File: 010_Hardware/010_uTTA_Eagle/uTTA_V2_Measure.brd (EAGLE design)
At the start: 100.4 x 79 mm, 304 parts, among them IC101.1 LT1167, IC101.2 LT1167, IC101.3 LT1167, IC101.4 LT1167, IC151.1 MCP602SN, IC151.3 MCP602SN, IC301 AD5664, IC302 LT1004CLP-2.5, IC303 TL074D, IC351.1 OPA2156ID, IC351.2 OPA2156ID, IC351.3 OPA2156ID, IC351.4 OPA2156ID, IC601.1 MAX6675ISA, IC601.2 MAX6675ISA, IC601.3 MAX6675ISA, IC601.4 MAX6675ISA, T151 BSS138PS, U11 NUCLEO_F103_BOT, U121.1 W25Q128JV, U121.2 W25Q128JV, X101.1 BU-SMA-GSPECIAL, X101.2 BU-SMA-GSPECIAL, X101.3 BU-SMA-GSPECIAL, X101.4 BU-SMA-GSPECIAL

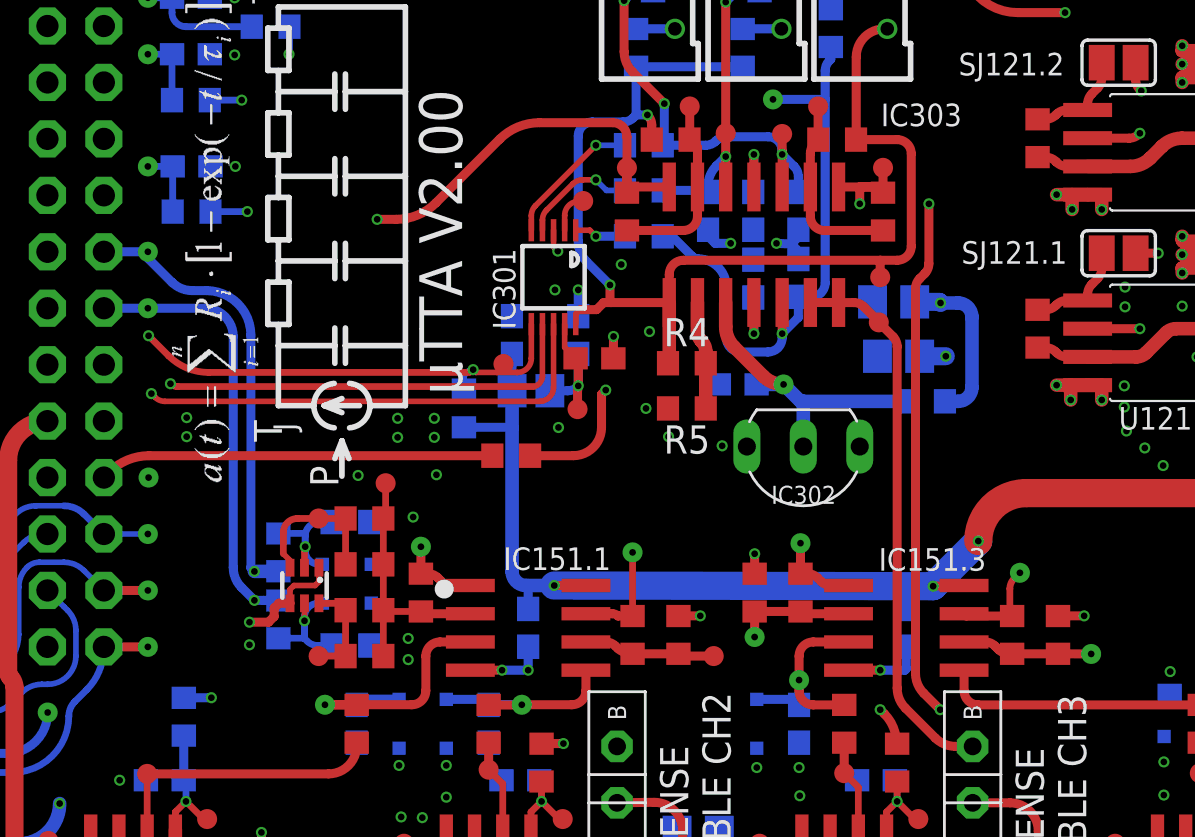
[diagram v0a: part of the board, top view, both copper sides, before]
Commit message: Optimization of Testpoints for Calibration
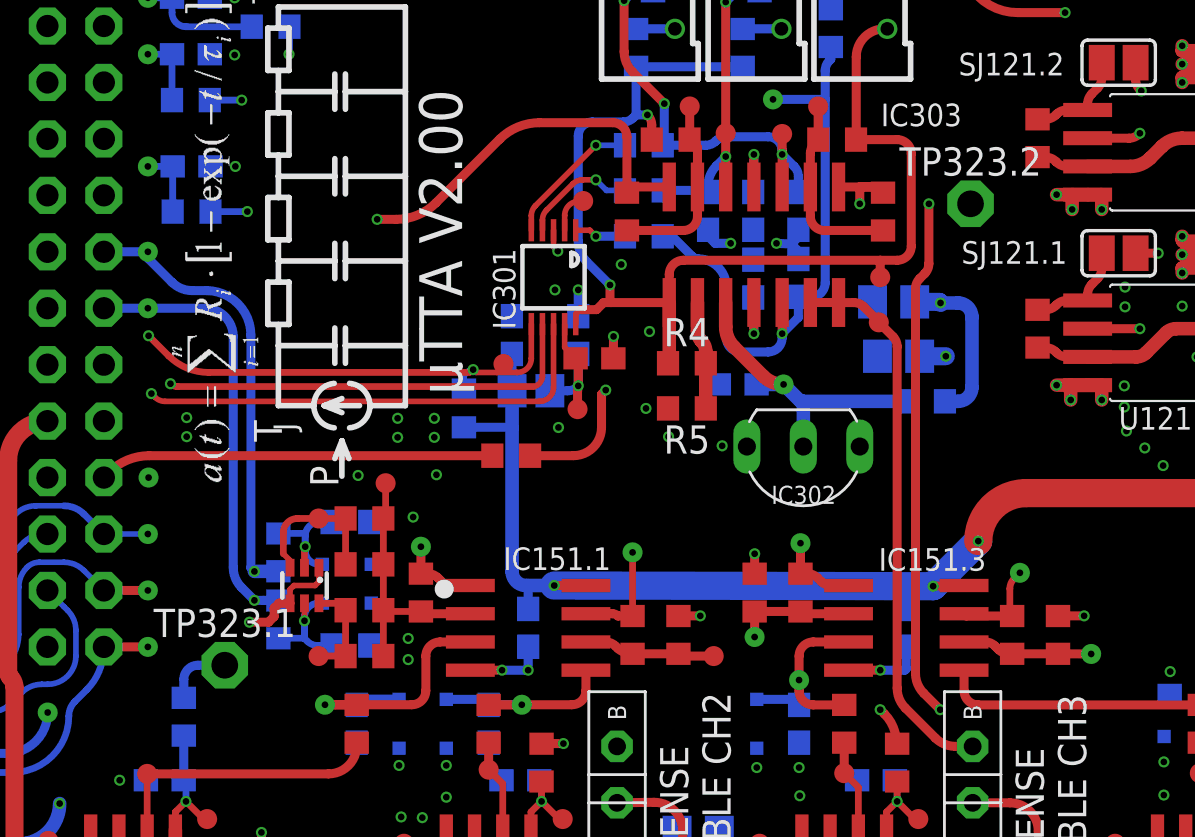
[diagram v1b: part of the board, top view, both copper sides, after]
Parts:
- IC351.1, IC351.2, IC351.3, IC351.4: value OPA2156ID -> AD8672ARZ
- R326.1, R326.2: value 2k -> 4k99
- TP1, TP101.1, TP101.2, TP101.3, TP101.4, TP102.1, TP102.2, TP102.3, TP102.4, TP103.1, TP103.2, TP103.3, TP103.4, TP104.1, TP104.2, TP104.3, TP104.4, TP105.1, TP105.2, TP105.3, TP105.4, TP107.1, TP107.2, TP107.3, TP107.4, TP152.1, TP152.2, TP153, TP154, TP301, TP302, TP304, TP306, TP321.1, TP321.2, TP322.1, TP322.2, TP351.1, TP351.2, TP351.3, TP351.4, TP352.1, TP352.2, TP352.3, TP352.4, TP353.1, TP353.2, TP353.3, TP353.4, TP354.2, TP354.3, TP354.4, TP355.1, TP355.2, TP355.3, TP355.4, TP9354.1: value TP -> TPC90
- TP323.1, TP323.2: value TP -> TPO210H120; device A_Testpoint:C90 -> A_Testpoint:P1-13
- moved TP323.1 28.8 mm to (28.7, 30.7), turned to 0 degrees
- moved TP323.2 4.26 mm to (62.3, 51.5), turned to 0 degrees
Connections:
- removed net V_OFF1: IC303.7, R103.1.1, R326.1.1, TP323.1.P$1
- removed net V_OFF2_4: IC303.1, R103.2.1, R103.3.1, R103.4.1, R326.2.1, TP323.2.P$1
- new net V_OFF0: IC303.7, R103.1.1, R326.1.1, TP323.1.1
- new net V_OFF1_3: IC303.1, R103.2.1, R103.3.1, R103.4.1, R326.2.1, TP323.2.1
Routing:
- net V_OFF1_3: track 0.00 -> 68.7 mm, vias 0 -> 6
- net V_OFF2_4: track 67.7 -> 0.00 mm, vias 6 -> 0
- net V_OFF1: track 47.3 -> 0.00 mm, vias 2 -> 0
- net V_OFF0: track 0.00 -> 47.0 mm, vias 0 -> 1
- net AGND: vias 310 -> 309
